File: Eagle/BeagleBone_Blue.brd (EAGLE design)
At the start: 86.4 x 54.6 mm, 297 parts, among them M1 JST_ZH_2, M2 JST_ZH_2, M3 JST_ZH_2, M4 JST_ZH_2, P10 SCHA5B0200, Q3 MOSFET-N, U1 TPD4S012_DRY_6, U4 TPD4S012_DRY_6, U5 24LC_32AT-I/OT, U6 SN74LVC1G07_DCK_5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

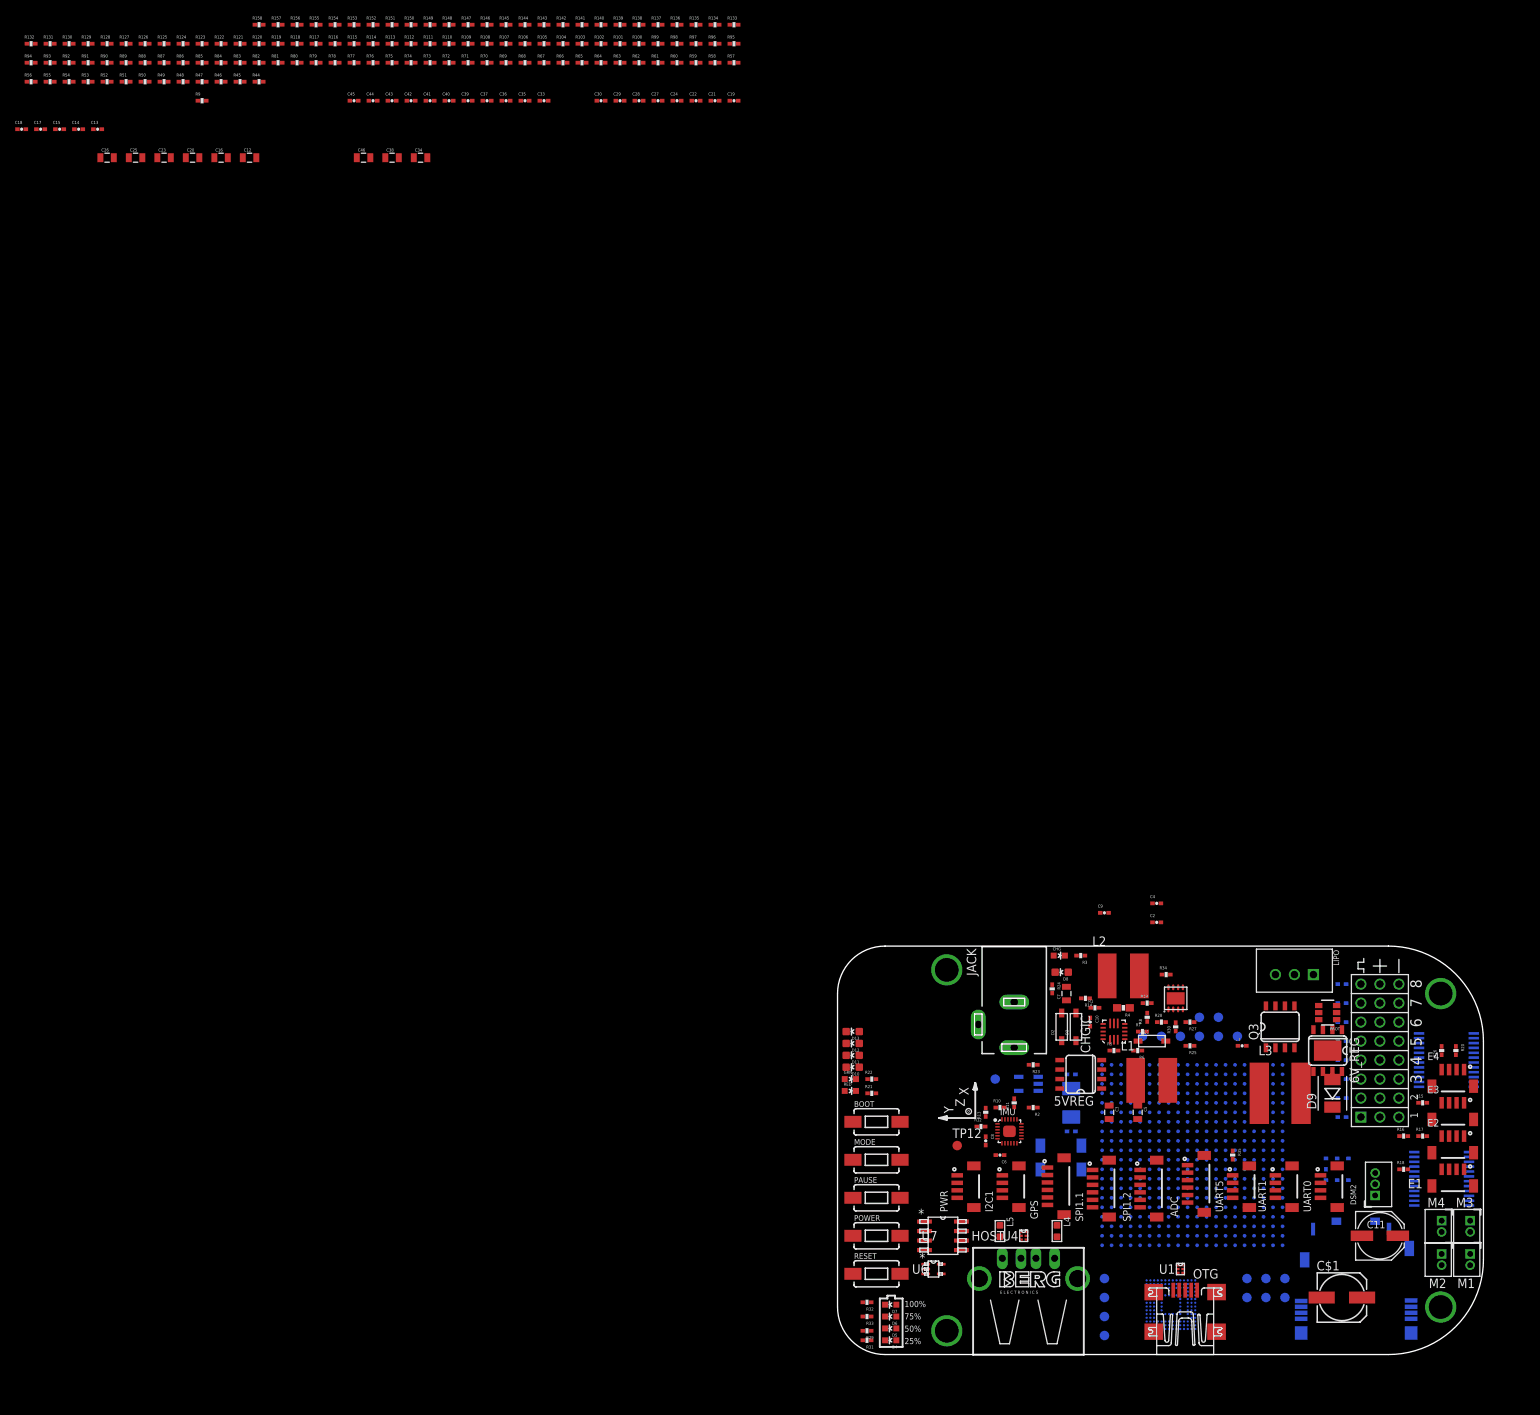
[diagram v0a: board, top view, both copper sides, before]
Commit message: Rough placed a bunch of parts
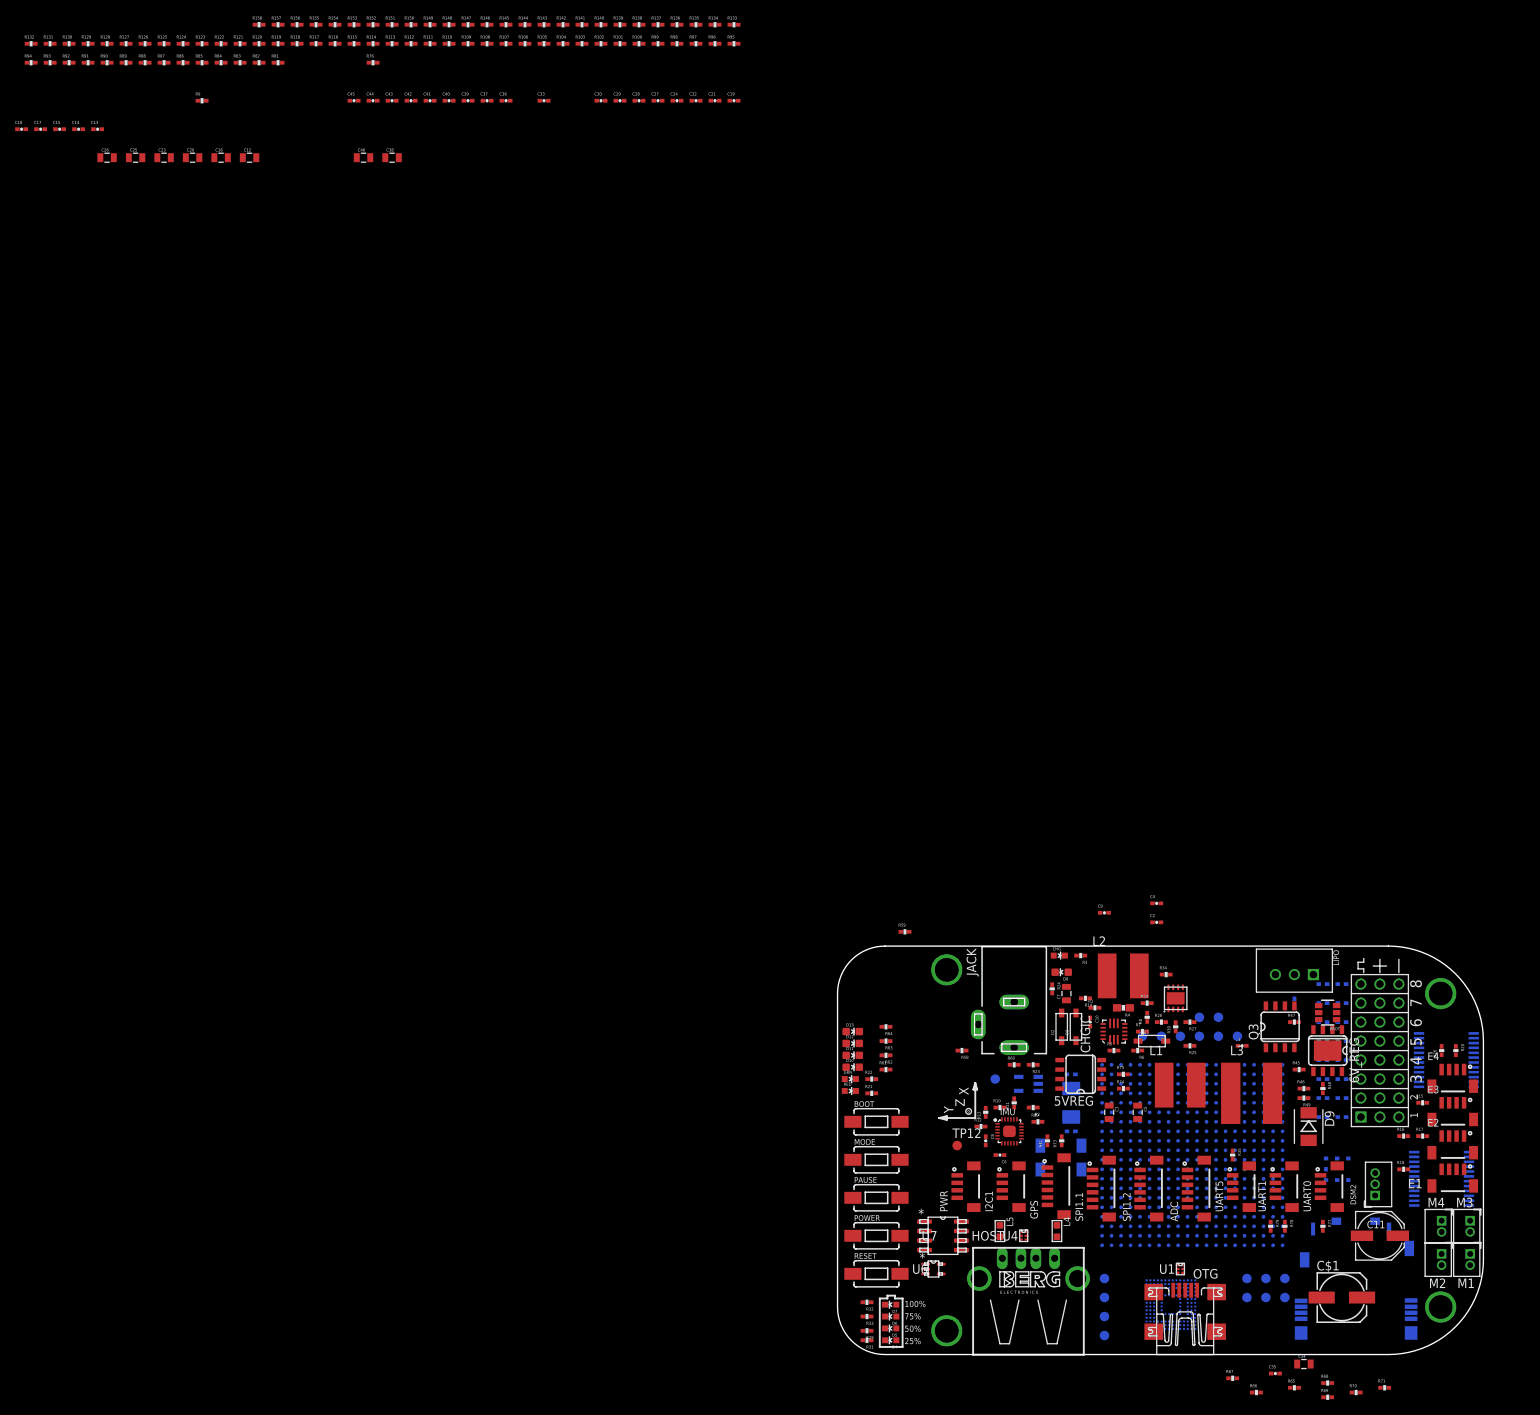
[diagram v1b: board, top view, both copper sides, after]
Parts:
- moved R71 215.4 mm to (73.0, -59.1)
- moved R70 212.4 mm to (69.2, -59.7)
- moved R56 212.2 mm to (64.8, -7.62), flipped to the bottom, turned to 180 degrees
- moved R55 211.6 mm to (64.8, -10.2), flipped to the bottom, turned to 180 degrees
- moved R54 211.1 mm to (64.8, -12.7), flipped to the bottom, turned to 180 degrees
- moved R53 210.6 mm to (64.8, -15.2), flipped to the bottom, turned to 180 degrees
- moved R52 210.3 mm to (64.8, -17.8), flipped to the bottom
- moved R51 209.9 mm to (64.8, -20.3), flipped to the bottom
- moved R50 209.7 mm to (64.8, -22.9), flipped to the bottom
- moved R69 209.5 mm to (65.4, -60.3)
- moved R68 206.6 mm to (65.4, -58.4)
- moved R49 204.2 mm to (62.2, -20.3), turned to 180 degrees
- moved R48 203.3 mm to (64.8, -19.1), turned to 270 degrees
- moved R77 202.4 mm to (64.8, -37.5), turned to 270 degrees
- moved R79 201.2 mm to (57.8, -37.5), turned to 270 degrees
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
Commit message: Rough placed a few parts
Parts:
- moved R59 42.4 mm to (50.2, -7.62)
- moved R66 24.0 mm to (74.9, -45.1)
- moved R71 20.2 mm to (64.8, -40.6), turned to 90 degrees
- moved R65 18.0 mm to (73.7, -46.4)
- moved C35 17.6 mm to (73.7, -48.3)
- moved R67 15.1 mm to (59.7, -44.5)
- moved C1 13.9 mm to (47.0, -1.27)
- moved R68 12.3 mm to (58.4, -48.3)
- moved R69 12.3 mm to (58.4, -50.2)
- moved R70 10.5 mm to (73.7, -50.2)
- moved C34 7.10 mm to (68.6, -52.7)
- moved C2 2.62 mm to (45.1, 2.54)

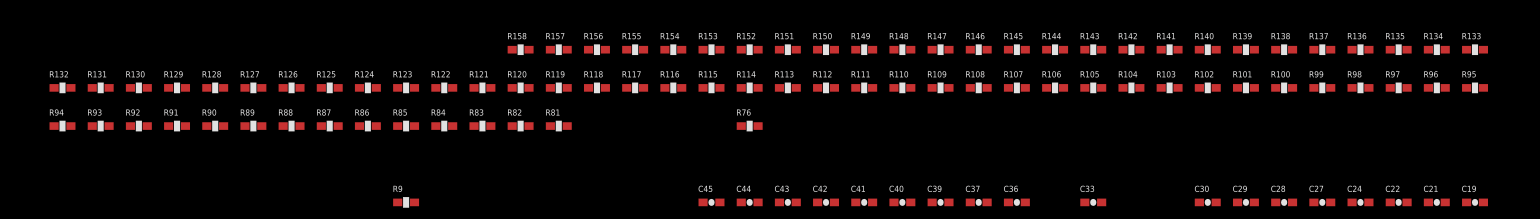
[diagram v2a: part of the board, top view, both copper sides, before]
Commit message: Remove SYS_BOOT DNI resistors
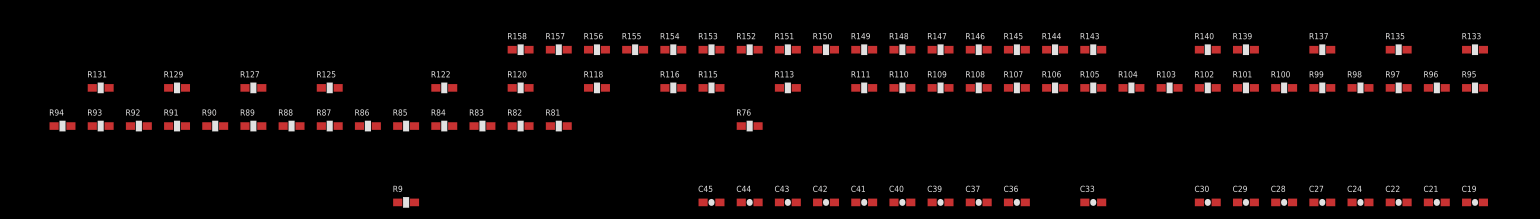
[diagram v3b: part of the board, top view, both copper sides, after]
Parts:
- removed R112, R114, R117, R119, R121, R123, R124, R126, R128, R130, R132, R134, R136, R138, R141, R142: 100K,1%,DNI, Strawson_Eagle_Lib:0402-RES
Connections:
- net GND: no longer R117.1, R119.1, R121.1, R123.1, R141.1
- net LED_2: no longer R142.1
- net MDIR_2B: no longer R141.2
- net MDIR_3A: no longer R119.2
- net MDIR_3B: no longer R117.2
- net MDIR_4A: no longer R112.1
- net MDIR_4B: no longer R114.1
- net N$141: no longer R128.1
- net N$144: no longer R130.1
- net N$150: no longer R134.1
- net N$153: no longer R136.1
- net N$156: no longer R138.1
- net SERVO_EN: no longer R132.1
- net SVO5: no longer R124.1
- net SVO6: no longer R126.1
- net SVO7: no longer R121.2
- net SVO8: no longer R123.2
- net VDD_3V3A: no longer R112.2, R114.2, R124.2, R126.2, R128.2, R130.2, R132.2, R134.2, R136.2, R138.2, R142.2

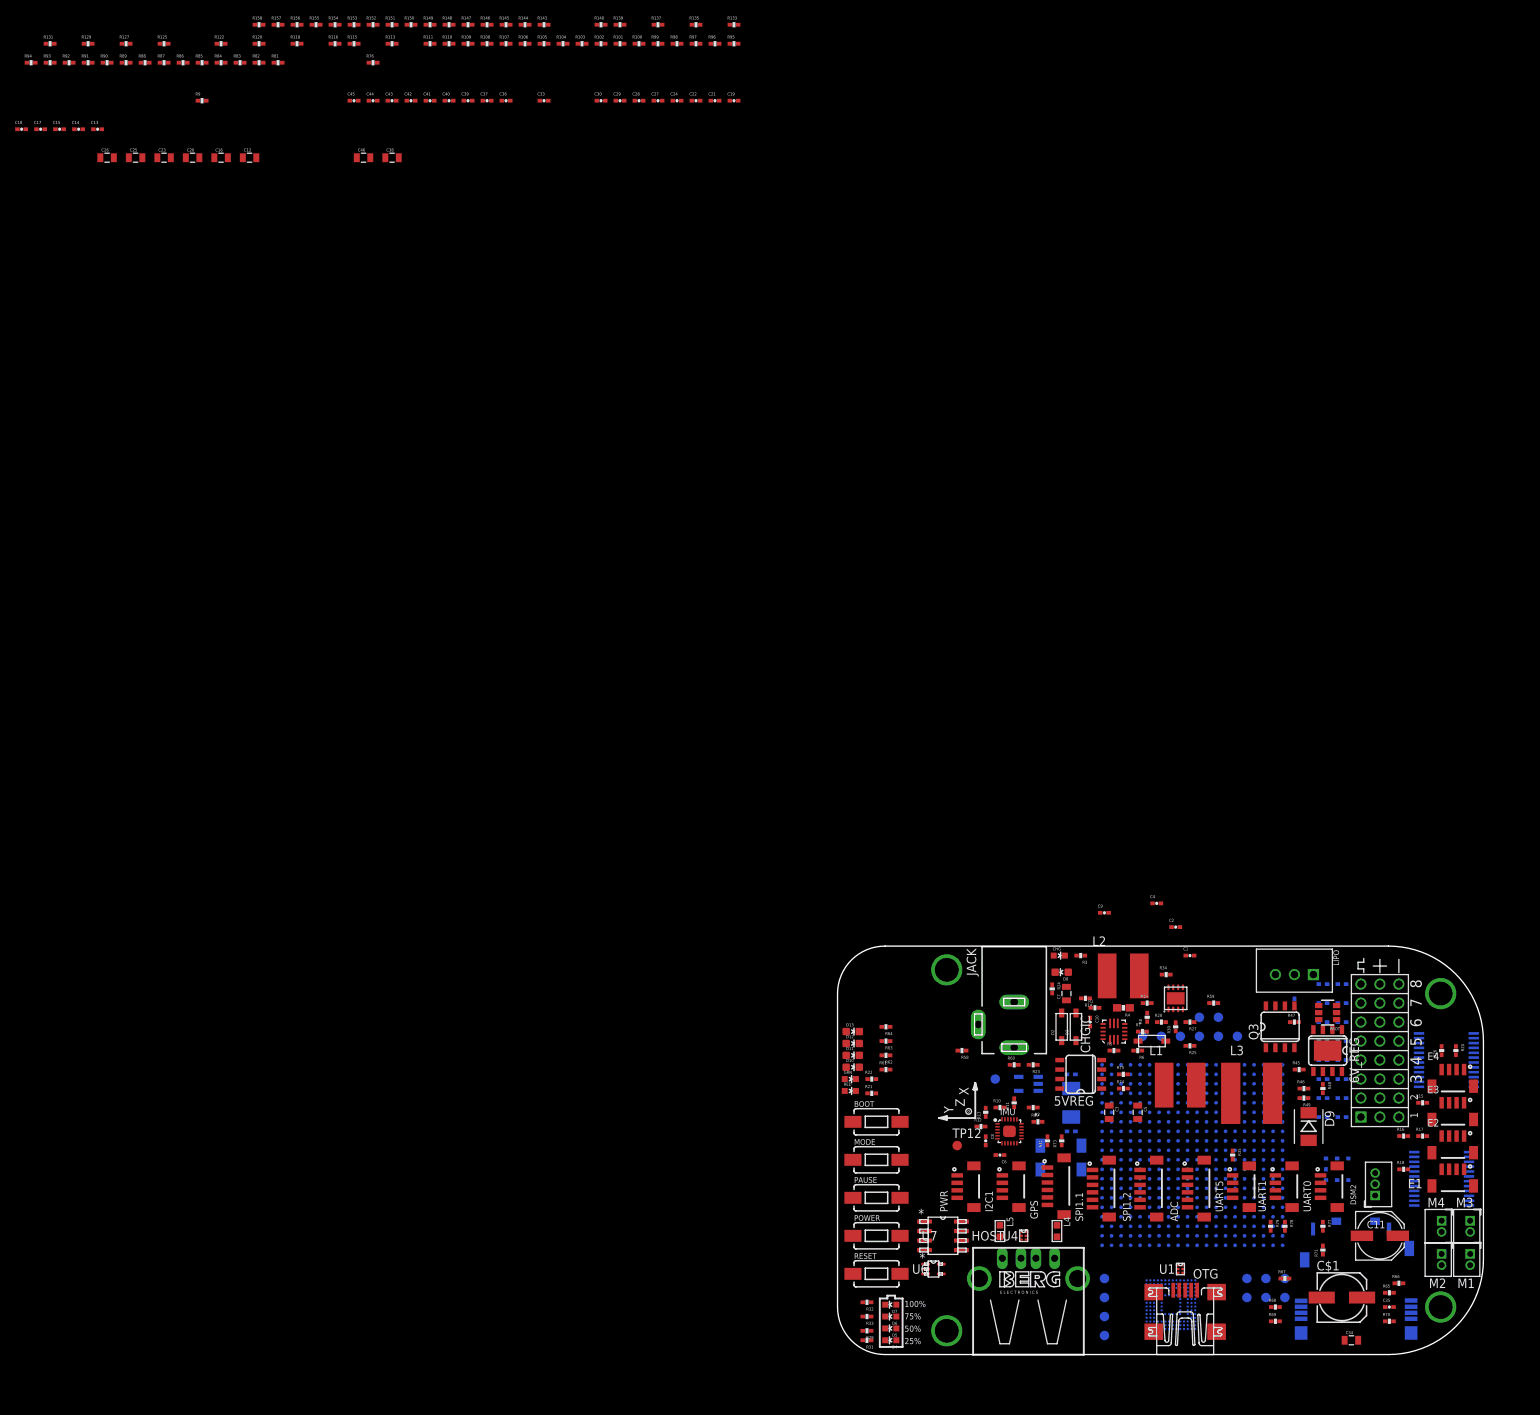
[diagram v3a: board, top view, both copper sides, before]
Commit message: Rough placed a few parts and print schematic
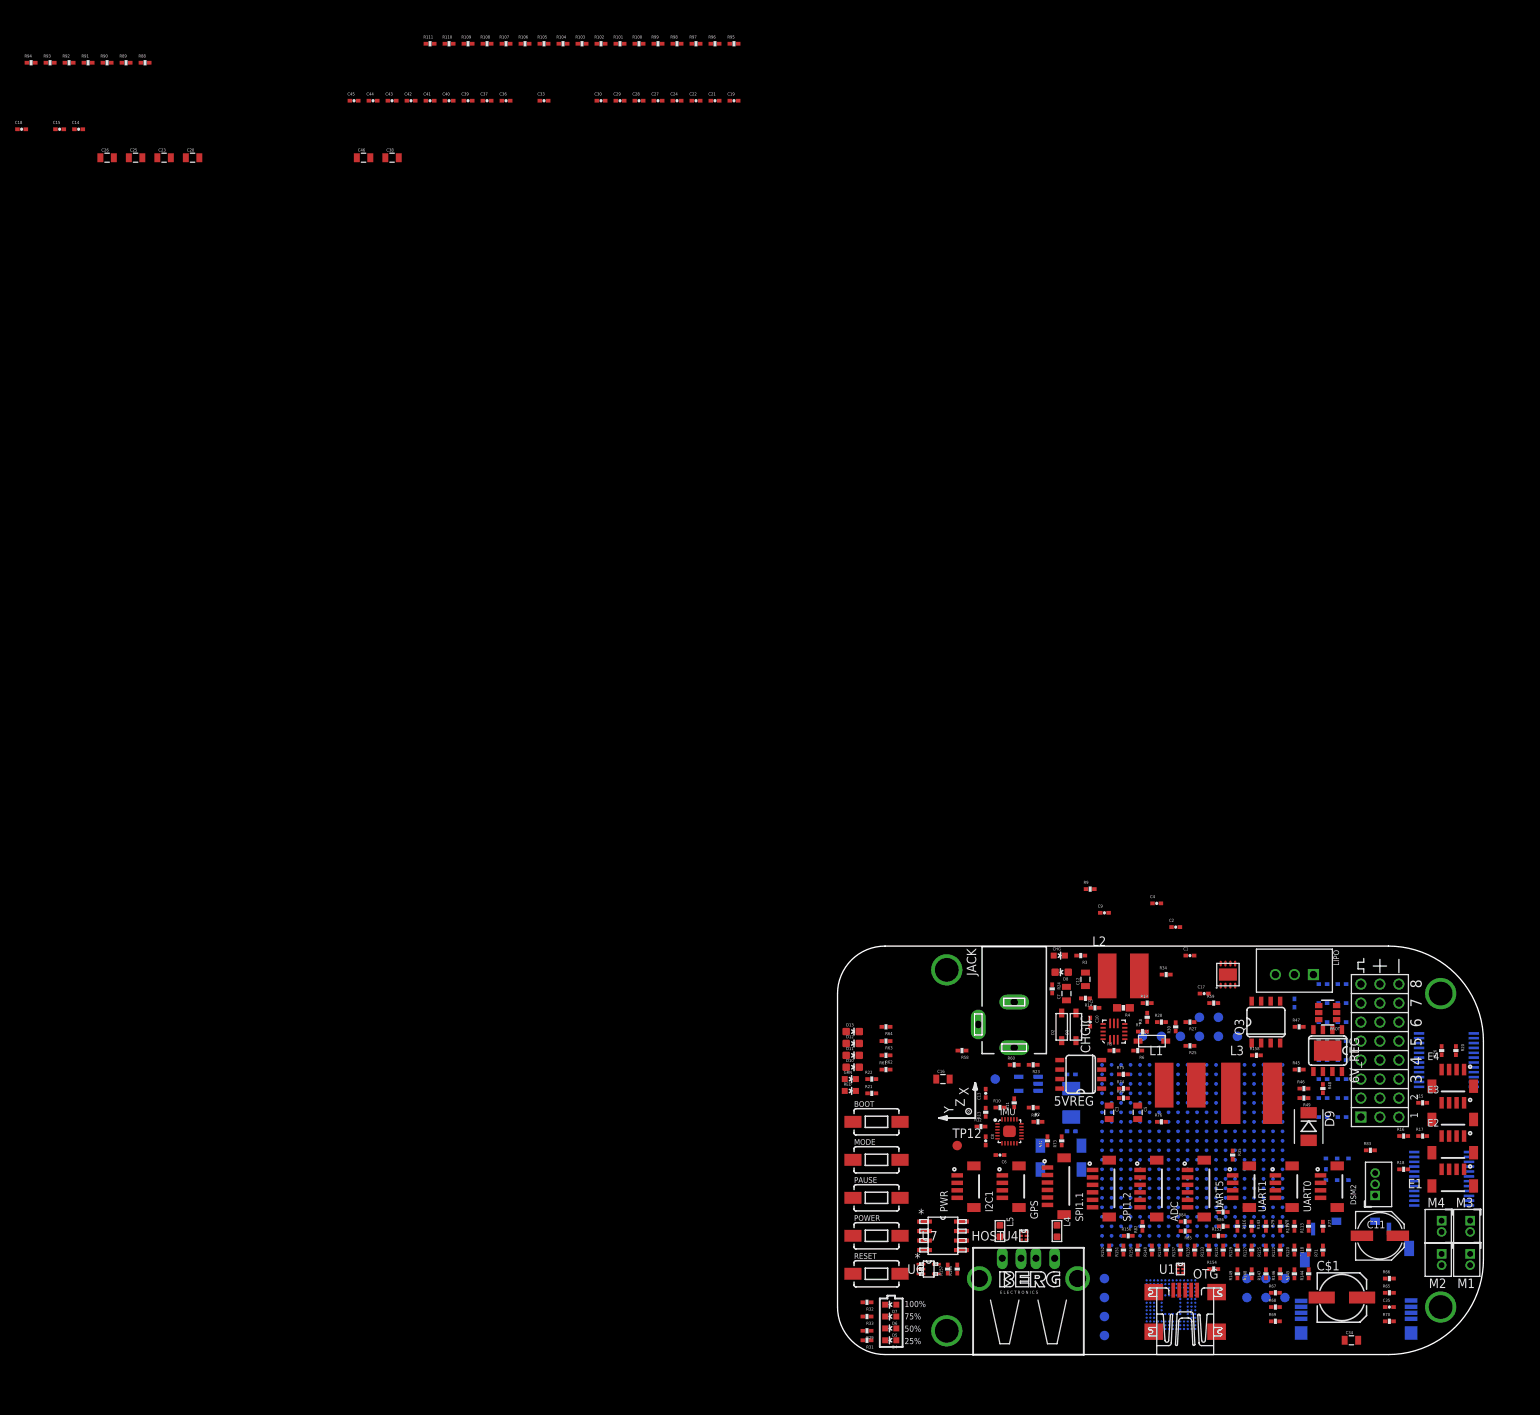
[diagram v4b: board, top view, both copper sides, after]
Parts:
- moved R131 225.0 mm to (51.4, -40.6), turned to 90 degrees
- moved R129 222.8 mm to (53.3, -40.6), turned to 90 degrees
- moved R127 220.6 mm to (55.2, -40.6), turned to 90 degrees
- moved R125 218.4 mm to (57.1, -40.6), turned to 90 degrees
- moved R122 214.6 mm to (59.1, -40.6), turned to 90 degrees
- moved R120 212.5 mm to (61.0, -40.6), turned to 90 degrees
- moved R118 210.5 mm to (62.9, -40.6), turned to 90 degrees
- moved R83 209.7 mm to (71.1, -27.3)
- moved R87 209.0 mm to (51.4, -35.6)
- moved R86 208.7 mm to (51.4, -37.5)
- moved R85 204.2 mm to (46.4, -38.1), turned to 180 degrees
- moved R154 203.7 mm to (50.2, -43.2)
- moved R115 202.0 mm to (61.0, -37.5), turned to 90 degrees
- moved R84 201.6 mm to (46.4, -36.8)
- moved R113 200.1 mm to (62.9, -37.5), turned to 90 degrees
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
